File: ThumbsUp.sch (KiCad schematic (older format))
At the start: 170 parts, among them IC1 RP2040, IC2 W25Q128JVSIM, IC3 RP2040, IC4 W25Q128JVSIM, J1 Conn_01x04_Male, J10 Raiser_Male, J11 Raiser_Female, J12 Raiser_Male, J13 Raiser_Female, J14 Raiser_Male, J15 Raiser_Female, J16 Raiser_Male, J17 Raiser_Female, J18 Raiser_Male, J19 Raiser_Female, J2 Conn_01x04_Male, J20 Conn_01x04_Female, J21 Conn_01x04_Female, J22 Conn_01x04_Female, J23 Conn_01x04_Female, J24 Conn_01x04_Male, J25 Conn_01x04_Male, J26 Conn_01x04_Male, J27 Conn_01x04_Male, J28 Conn_01x04_Female, J29 Conn_01x04_Female, J3 Conn_01x04_Female, J30 Conn_01x04_Female, J31 Conn_01x04_Female, J32 USB_C_Receptacle_USB2.0, J33 Raiser_Male, J34 Raiser_Female, J35 Raiser_Male, J36 STX-3501-3N, J37 USB_C_Receptacle_USB2.0, J38 Raiser_Female, J39 Raiser_Male, J4 Conn_01x04_Male, J40 Raiser_Female, J41 Raiser_Male, J42 Raiser_Female, J43 Raiser_Male, J44 Raiser_Female, J45 Raiser_Male, J46 STX-3501-3N, J47 Raiser_Female, J48 Raiser_Male, J49 Raiser_Female, J5 Conn_01x04_Female, J50 Raiser_Male, J51 Raiser_Female, J52 Raiser_Male, J6 Conn_01x04_Male, J7 Conn_01x04_Male, J8 Conn_01x04_Male, J9 Raiser_Female, U1 AMS1117-3.3_SOT223, U2 AMS1117-3.3_SOT223, Y1 ABLS-12.000MHZ-B4-T, Y2 ABLS-12.000MHZ-B4-T

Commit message: Wired both RP2040s
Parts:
- MX1, MX10, MX11, MX12, MX13, MX14, MX15, MX16, MX17, MX18, MX19, MX2, MX20, MX21, MX22, MX23, MX24, MX25, MX26, MX27, MX28, MX29, MX3, MX30, MX31, MX32, MX33, MX34, MX35, MX36, MX37, MX38, MX39, MX4, MX40, MX41, MX42, MX43, MX44, MX45, MX46, MX47, MX48, MX49, MX5, MX50, MX51, MX52, MX53, MX54, MX55, MX56, MX57, MX58, MX6, MX7, MX8, MX9: footprint MX_Alps_Hybrid:MX-1U-NoLED_HotSwap -> keyswitches:MX-GLP2-HotSwap

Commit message: Layed out tracks on L2
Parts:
- J36, J46: value STX-3501-3N -> PJ-3200B; footprint STX-3501-3N:STX35013N -> random-keyboard-parts:PJ-3200B-4A
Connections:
- net +5V: now also J36.2, J46.2; no longer J36.3, J46.3
- net GND: now also J1.3 (Pin_3), J1.4 (Pin_4)
- net K_5: no longer J39.1 (Pin_1)
- net K_WIN: no longer J1.1 (Pin_1)
- net L-TIP: now also J36.3; no longer J36.2
- net R-TIP: now also J46.3; no longer J46.2
- no-connect marks 84 -> 91
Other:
- moved on the sheet: J36, J46
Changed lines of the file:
@@
 Wire Wire Line
 	8150 12700 8150 13500
-Connection ~ 8150 11900
-Wire Wire Line
-	8150 11900 8150 12700
 Connection ~ 10350 11850
 Wire Wire Line
@@
 	5200 5750 3950 5750
 Connection ~ 3950 5750
-Wire Wire Line
-	5200 8000 5200 7100
 Connection ~ 5200 7100
 $Comp
@@
 Text GLabel 7250 12100 0    50   Input ~ 0
 K_R
-Text GLabel 7950 12100 0    50   Input ~ 0
-K_T
 Text GLabel 7250 12900 0    50   Input ~ 0
 K_F
@@
 Connection ~ 14250 5700
 Wire Wire Line
-	14550 7950 15500 7950
-Wire Wire Line
 	15500 7950 15500 7050
 Connection ~ 15500 7050
@@
 	1    0    0    1
 $EndComp
-$Comp
-L STX-3501-3N:STX-3501-3N J46
-U 1 1 63F7C0D7
-P 15450 8050
-F 0 "J46" V 15804 8178 50  0000 L CNN
-F 1 "STX-3501-3N" V 15895 8178 50  0000 L CNN
-F 2 "STX-3501-3N:STX35013N" H 16100 8150 50  0001 L CNN
-F 3 "https://datasheet.datasheetarchive.com/originals/distributors/Datasheets_SAMA/ae9d1df0991347f2f81145ba35ca04dc.pdf" H 16100 8050 50  0001 L CNN
-F 4 "Phone Connectors 3.5mm S LUGS STEREO 3P THRU HOLE" H 16100 7950 50  0001 L CNN "Description"
-F 5 "5" H 16100 7850 50  0001 L CNN "Height"
-F 6 "Kycon" H 16100 7750 50  0001 L CNN "Manufacturer_Name"
-F 7 "STX-3501-3N" H 16100 7650 50  0001 L CNN "Manufacturer_Part_Number"
-F 8 "806-STX-3501-3N" H 16100 7550 50  0001 L CNN "Mouser Part Number"
-F 9 "https://www.mouser.co.uk/ProductDetail/Kycon/STX-3501-3N?qs=BBNwCsfFaznpJt4o1Jp%2FTg%3D%3D" H 16100 7450 50  0001 L CNN "Mouser Price/Stock"
-F 10 "" H 16100 7350 50  0001 L CNN "Arrow Part Number"
-F 11 "" H 16100 7250 50  0001 L CNN "Arrow Price/Stock"
-F 12 "" H 16100 7150 50  0001 L CNN "Mouser Testing Part Number"
-F 13 "" H 16100 7050 50  0001 L CNN "Mouser Testing Price/Stock"
-	1    15450 8050
-	0    1    1    0
-$EndComp
-$Comp
-L power:GND #PWR0149
-U 1 1 641658E3
-P 5500 8100
-F 0 "#PWR0149" H 5500 7850 50  0001 C CNN
-F 1 "GND" H 5505 7927 50  0000 C CNN
-F 2 "" H 5500 8100 50  0001 C CNN
-F 3 "" H 5500 8100 50  0001 C CNN
-	1    5500 8100
-	1    0    0    -1
-$EndComp
-Wire Wire Line
-	5300 8100 5500 8100
-Wire Wire Line
-	5300 8900 5500 8900
 Text GLabel 5050 8100 3    50   Input ~ 0
 L-TIP
-Text GLabel 5500 8100 2    50   Input ~ 0
-L-BASE
-Text GLabel 5500 8900 2    50   Input ~ 0
-L-RING1
-$Comp
-L power:GND #PWR0152
-U 1 1 64226D4D
-P 15700 8050
-F 0 "#PWR0152" H 15700 7800 50  0001 C CNN
-F 1 "GND" H 15705 7877 50  0000 C CNN
-F 2 "" H 15700 8050 50  0001 C CNN
-F 3 "" H 15700 8050 50  0001 C CNN
-	1    15700 8050
-	1    0    0    -1
-$EndComp
-Wire Wire Line
-	15450 8050 15700 8050
-Wire Wire Line
-	15450 8850 15700 8850
 Text GLabel 15100 8050 1    50   Input ~ 0
 R-TIP
-Text GLabel 15700 8050 2    50   Input ~ 0
-R-BASE
-Text GLabel 15700 8850 2    50   Input ~ 0
+Text GLabel 16250 7950 2    50   Input ~ 0
 R-RING1
 $Comp
@@
 $EndComp
 $Comp
-L power:+5V #PWR0147
-U 1 1 63F119E5
-P 5300 8900
-F 0 "#PWR0147" H 5300 8750 50  0001 C CNN
-F 1 "+5V" H 5315 9073 50  0000 C CNN
-F 2 "" H 5300 8900 50  0001 C CNN
-F 3 "" H 5300 8900 50  0001 C CNN
-	1    5300 8900
-	-1   0    0    1
-$EndComp
-Connection ~ 5300 8900
-Wire Wire Line
-	4250 8000 5200 8000
-$Comp
-L STX-3501-3N:STX-3501-3N J36
-U 1 1 63D573AD
-P 5300 8100
-F 0 "J36" V 5654 8228 50  0000 L CNN
-F 1 "STX-3501-3N" V 5745 8228 50  0000 L CNN
-F 2 "STX-3501-3N:STX35013N" H 5950 8200 50  0001 L CNN
-F 3 "https://datasheet.datasheetarchive.com/originals/distributors/Datasheets_SAMA/ae9d1df0991347f2f81145ba35ca04dc.pdf" H 5950 8100 50  0001 L CNN
-F 4 "Phone Connectors 3.5mm S LUGS STEREO 3P THRU HOLE" H 5950 8000 50  0001 L CNN "Description"
-F 5 "5" H 5950 7900 50  0001 L CNN "Height"
-F 6 "Kycon" H 5950 7800 50  0001 L CNN "Manufacturer_Name"
-F 7 "STX-3501-3N" H 5950 7700 50  0001 L CNN "Manufacturer_Part_Number"
-F 8 "806-STX-3501-3N" H 5950 7600 50  0001 L CNN "Mouser Part Number"
-F 9 "https://www.mouser.co.uk/ProductDetail/Kycon/STX-3501-3N?qs=BBNwCsfFaznpJt4o1Jp%2FTg%3D%3D" H 5950 7500 50  0001 L CNN "Mouser Price/Stock"
-F 10 "" H 5950 7400 50  0001 L CNN "Arrow Part Number"
-F 11 "" H 5950 7300 50  0001 L CNN "Arrow Price/Stock"
-F 12 "" H 5950 7200 50  0001 L CNN "Mouser Testing Part Number"
-F 13 "" H 5950 7100 50  0001 L CNN "Mouser Testing Price/Stock"
-	1    5300 8100
-	0    1    1    0
-$EndComp
-$Comp
 L power:+5V #PWR0148
 U 1 1 63FA1289
-P 15450 8850
-F 0 "#PWR0148" H 15450 8700 50  0001 C CNN
-F 1 "+5V" H 15465 9023 50  0000 C CNN
-F 2 "" H 15450 8850 50  0001 C CNN
-F 3 "" H 15450 8850 50  0001 C CNN
-	1    15450 8850
-	-1   0    0    1
+P 16150 7950
+F 0 "#PWR0148" H 16150 7800 50  0001 C CNN
+F 1 "+5V" H 16165 8123 50  0000 C CNN
+F 2 "" H 16150 7950 50  0001 C CNN
+F 3 "" H 16150 7950 50  0001 C CNN
+	1    16150 7950
+	1    0    0    -1
 $EndComp
-Connection ~ 15450 8850
 $Comp
 L Device:R R4
@@
 $EndComp
 Connection ~ 15000 8050
-Wire Wire Line
-	15000 8050 15350 8050
-Wire Wire Line
-	14550 8050 15000 8050
 Text GLabel 14550 7850 2    50   Input ~ 0
 K_BSPC
@@
 	8150 10800 8350 10800
 Connection ~ 8150 10800
-Wire Wire Line
-	8150 11100 8150 11900
 Text GLabel 6350 12400 2    50   Input ~ 0
 K_GRAVE
@@
 $EndComp
 Connection ~ 14500 15800
-Text GLabel 5600 15050 2    50   Input ~ 0
-K_WIN
 NoConn ~ 3450 9200
 NoConn ~ 3550 9200
@@
 	4250 8100 4850 8100
 Connection ~ 4850 8100
-Wire Wire Line
-	4850 8100 5200 8100
 Text GLabel 4250 7800 2    50   Input ~ 0
 K_3
@@
 Text GLabel 3750 9200 3    50   Input ~ 0
 K_4
-Text GLabel 20550 10400 3    50   Input ~ 0
-K_5
 $Comp
 L Connector:Conn_01x04_Female J51
@@
 Text GLabel 14550 8350 2    50   Input ~ 0
 K_THR
+$Comp
+L power:+5V #PWR0147
+U 1 1 63F119E5
+P 6000 8000
+F 0 "#PWR0147" H 6000 7850 50  0001 C CNN
+F 1 "+5V" H 6015 8173 50  0000 C CNN
+F 2 "" H 6000 8000 50  0001 C CNN
+F 3 "" H 6000 8000 50  0001 C CNN
+	1    6000 8000
+	1    0    0    -1
+$EndComp
+Text GLabel 6200 8000 2    50   Input ~ 0
+L-RING1
+Wire Wire Line
+	6000 8000 6200 8000
+Text GLabel 6200 8100 2    50   Input ~ 0
+L-BASE
+Wire Wire Line
+	6000 8100 6200 8100
+$Comp
+L power:GND #PWR0149
+U 1 1 641658E3
+P 6000 8100
+F 0 "#PWR0149" H 6000 7850 50  0001 C CNN
+F 1 "GND" H 6005 7927 50  0000 C CNN
+F 2 "" H 6000 8100 50  0001 C CNN
+F 3 "" H 6000 8100 50  0001 C CNN
+	1    6000 8100
+	1    0    0    -1
+$EndComp
+Wire Wire Line
+	5200 8000 5200 7100
+Wire Wire Line
+	4250 8000 5200 8000
+Wire Wire Line
+	4850 8100 5200 8100
+$Comp
+L power:GND #PWR0152
+U 1 1 64226D4D
+P 16150 8050
+F 0 "#PWR0152" H 16150 7800 50  0001 C CNN
+F 1 "GND" H 16155 7877 50  0000 C CNN
+F 2 "" H 16150 8050 50  0001 C CNN
+F 3 "" H 16150 8050 50  0001 C CNN
+	1    16150 8050
+	1    0    0    -1
+$EndComp
+Text GLabel 16250 8050 2    50   Input ~ 0
+R-BASE
+$Comp
+L STX-3501-3N:STX-3501-3N J36
+U 1 1 63D573AD
+P 6000 8100
+F 0 "J36" V 6354 8228 50  0000 L CNN
+F 1 "PJ-3200B" V 6445 8228 50  0000 L CNN
+F 2 "random-keyboard-parts:PJ-3200B-4A" H 6650 8200 50  0001 L CNN
+F 3 "https://datasheet.datasheetarchive.com/originals/distributors/Datasheets_SAMA/ae9d1df0991347f2f81145ba35ca04dc.pdf" H 6650 8100 50  0001 L CNN
+F 4 "Phone Connectors 3.5mm S LUGS STEREO 3P THRU HOLE" H 6650 8000 50  0001 L CNN "Description"
+F 5 "5" H 6650 7900 50  0001 L CNN "Height"
+F 6 "Kycon" H 6650 7800 50  0001 L CNN "Manufacturer_Name"
+F 7 "STX-3501-3N" H 6650 7700 50  0001 L CNN "Manufacturer_Part_Number"
+F 8 "806-STX-3501-3N" H 6650 7600 50  0001 L CNN "Mouser Part Number"
+F 9 "https://www.mouser.co.uk/ProductDetail/Kycon/STX-3501-3N?qs=BBNwCsfFaznpJt4o1Jp%2FTg%3D%3D" H 6650 7500 50  0001 L CNN "Mouser Price/Stock"
+F 10 "" H 6650 7400 50  0001 L CNN "Arrow Part Number"
+F 11 "" H 6650 7300 50  0001 L CNN "Arrow Price/Stock"
+F 12 "" H 6650 7200 50  0001 L CNN "Mouser Testing Part Number"
+F 13 "" H 6650 7100 50  0001 L CNN "Mouser Testing Price/Stock"
+	1    6000 8100
+	-1   0    0    1
+$EndComp
+Wire Wire Line
+	15000 8050 15350 8050
+Wire Wire Line
+	14550 8050 15000 8050
+Wire Wire Line
+	14550 7950 15500 7950
+$Comp
+L STX-3501-3N:STX-3501-3N J46
+U 1 1 63F7C0D7
+P 16150 8050
+F 0 "J46" V 16504 8178 50  0000 L CNN
+F 1 "PJ-3200B" V 16595 8178 50  0000 L CNN
+F 2 "random-keyboard-parts:PJ-3200B-4A" H 16800 8150 50  0001 L CNN
+F 3 "https://datasheet.datasheetarchive.com/originals/distributors/Datasheets_SAMA/ae9d1df0991347f2f81145ba35ca04dc.pdf" H 16800 8050 50  0001 L CNN
+F 4 "Phone Connectors 3.5mm S LUGS STEREO 3P THRU HOLE" H 16800 7950 50  0001 L CNN "Description"
+F 5 "5" H 16800 7850 50  0001 L CNN "Height"
+F 6 "Kycon" H 16800 7750 50  0001 L CNN "Manufacturer_Name"
+F 7 "STX-3501-3N" H 16800 7650 50  0001 L CNN "Manufacturer_Part_Number"
+F 8 "806-STX-3501-3N" H 16800 7550 50  0001 L CNN "Mouser Part Number"
+F 9 "https://www.mouser.co.uk/ProductDetail/Kycon/STX-3501-3N?qs=BBNwCsfFaznpJt4o1Jp%2FTg%3D%3D" H 16800 7450 50  0001 L CNN "Mouser Price/Stock"
+F 10 "" H 16800 7350 50  0001 L CNN "Arrow Part Number"
+F 11 "" H 16800 7250 50  0001 L CNN "Arrow Price/Stock"
+F 12 "" H 16800 7150 50  0001 L CNN "Mouser Testing Part Number"
+F 13 "" H 16800 7050 50  0001 L CNN "Mouser Testing Price/Stock"
+	1    16150 8050
+	-1   0    0    1
+$EndComp
+Wire Wire Line
+	16150 8050 16250 8050
+Connection ~ 16150 8050
+Wire Wire Line
+	16150 7950 16250 7950
+Connection ~ 16150 7950
+Connection ~ 6000 8000
+Connection ~ 6000 8100
+Text GLabel 7950 12100 0    50   Input ~ 0
+K_T
+NoConn ~ 20550 10400
+Wire Wire Line
+	8150 11100 8150 11900
+Connection ~ 8150 11900
+Wire Wire Line
+	8150 11900 8150 12700
+NoConn ~ 5600 15050
+NoConn ~ 5600 15150
+NoConn ~ 4900 15100
+NoConn ~ 4900 15200
+NoConn ~ 4900 15300
+NoConn ~ 4900 15400
+Wire Wire Line
+	5600 15250 5600 15350
+$Comp
+L power:GND #PWR?
+U 1 1 6612E548
+P 5600 15350
+F 0 "#PWR?" H 5600 15100 50  0001 C CNN
+F 1 "GND" H 5605 15177 50  0000 C CNN
+F 2 "" H 5600 15350 50  0001 C CNN
+F 3 "" H 5600 15350 50  0001 C CNN
+	1    5600 15350
+	1    0    0    -1
+$EndComp
+Connection ~ 5600 15350
 $EndSCHEMATC

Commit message: Layed out tracks on R2
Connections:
- net GND: now also J39.1 (Pin_1), J39.2 (Pin_2), J39.3 (Pin_3), J39.4 (Pin_4), J41.3 (Pin_3), J41.4 (Pin_4), J52.1 (Pin_1)
- no-connect marks 91 -> 84
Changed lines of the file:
@@
-	0    1    1    0
-$EndComp
-$Comp
-L Connector:Conn_01x04_Male J41
-U 1 1 63F4665F
-P 20450 11050
-F 0 "J41" V 20512 11194 50  0000 L CNN
-F 1 "Raiser_Male" V 20603 11194 50  0000 L CNN
-F 2 "Connector_PinHeader_2.54mm:PinHeader_1x04_P2.54mm_Vertical" H 20450 11050 50  0001 C CNN
-F 3 "~" H 20450 11050 50  0001 C CNN
-	1    20450 11050
 	0    1    1    0
 $EndComp
@@
 NoConn ~ 20450 10700
 NoConn ~ 20550 10700
-NoConn ~ 20250 11250
-NoConn ~ 20350 11250
 NoConn ~ 20450 11250
 NoConn ~ 20550 11250
@@
 NoConn ~ 20450 9850
 NoConn ~ 20550 9850
-NoConn ~ 20250 10400
-NoConn ~ 20350 10400
-NoConn ~ 20450 10400
 $Comp
 L Connector:Conn_01x04_Female J42
@@
 NoConn ~ 18700 11250
 NoConn ~ 18800 11250
-NoConn ~ 18900 11250
 $Comp
 L Connector:Conn_01x04_Female J49
@@
 Text GLabel 7950 12100 0    50   Input ~ 0
 K_T
-NoConn ~ 20550 10400
 Wire Wire Line
 	8150 11100 8150 11900
@@
 	5600 15250 5600 15350
 $Comp
-L power:GND #PWR?
+L power:GND #PWR0157
 U 1 1 6612E548
 P 5600 15350
-F 0 "#PWR?" H 5600 15100 50  0001 C CNN
+F 0 "#PWR0157" H 5600 15100 50  0001 C CNN
 F 1 "GND" H 5605 15177 50  0000 C CNN
 F 2 "" H 5600 15350 50  0001 C CNN
@@
 $EndComp
 Connection ~ 5600 15350
+$Comp
+L power:GND #PWR0158
+U 1 1 64F744BC
+P 18900 11250
+F 0 "#PWR0158" H 18900 11000 50  0001 C CNN
+F 1 "GND" H 18905 11077 50  0000 C CNN
+F 2 "" H 18900 11250 50  0001 C CNN
+F 3 "" H 18900 11250 50  0001 C CNN
+	1    18900 11250
+	1    0    0    -1
+$EndComp
+$Comp
+L Connector:Conn_01x04_Male J41
+U 1 1 63F4665F
+P 20450 11050
+F 0 "J41" V 20512 11194 50  0000 L CNN
+F 1 "Raiser_Male" V 20603 11194 50  0000 L CNN
+F 2 "Connector_PinHeader_2.54mm:PinHeader_1x04_P2.54mm_Vertical" H 20450 11050 50  0001 C CNN
+F 3 "~" H 20450 11050 50  0001 C CNN
+	1    20450 11050
+	0    1    1    0
+$EndComp
+$Comp
+L power:GND #PWR0161
+U 1 1 64F7DEB1
+P 20250 11250
+F 0 "#PWR0161" H 20250 11000 50  0001 C CNN
+F 1 "GND" H 20255 11077 50  0000 C CNN
+F 2 "" H 20250 11250 50  0001 C CNN
+F 3 "" H 20250 11250 50  0001 C CNN
+	1    20250 11250
+	1    0    0    -1
+$EndComp
+Wire Wire Line
+	20350 11250 20250 11250
+Connection ~ 20250 11250
+Wire Wire Line
+	20250 10400 20350 10400
+Connection ~ 20350 10400
+Wire Wire Line
+	20350 10400 20450 10400
+Connection ~ 20450 10400
+Wire Wire Line
+	20450 10400 20550 10400
+$Comp
+L power:GND #PWR?
+U 1 1 651A673D
+P 20250 10400
+F 0 "#PWR?" H 20250 10150 50  0001 C CNN
+F 1 "GND" H 20255 10227 50  0000 C CNN
+F 2 "" H 20250 10400 50  0001 C CNN
+F 3 "" H 20250 10400 50  0001 C CNN
+	1    20250 10400
+	1    0    0    -1
+$EndComp
+Connection ~ 20250 10400
 $EndSCHEMATC

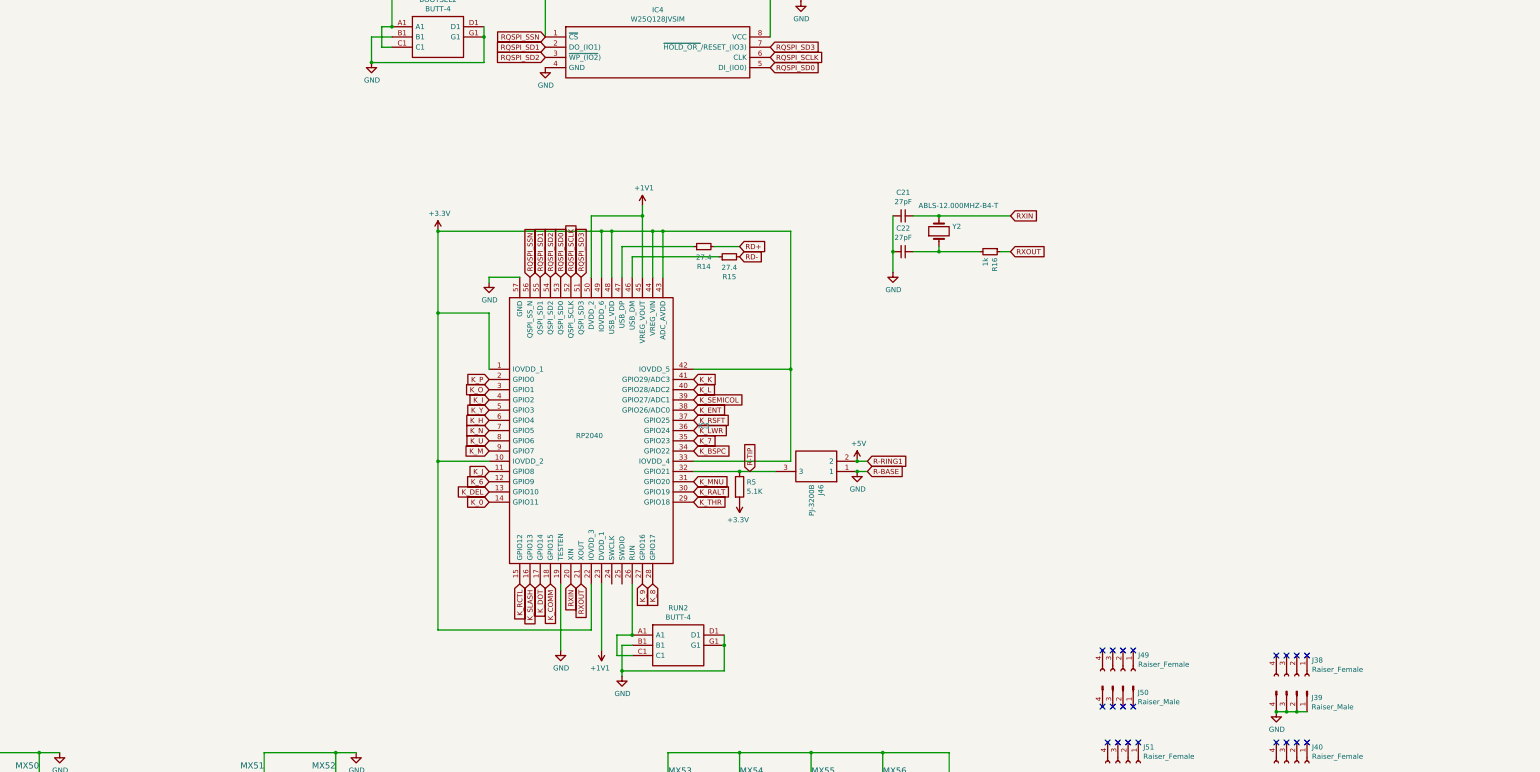
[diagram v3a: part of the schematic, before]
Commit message: Adding the 3key thumbclusters
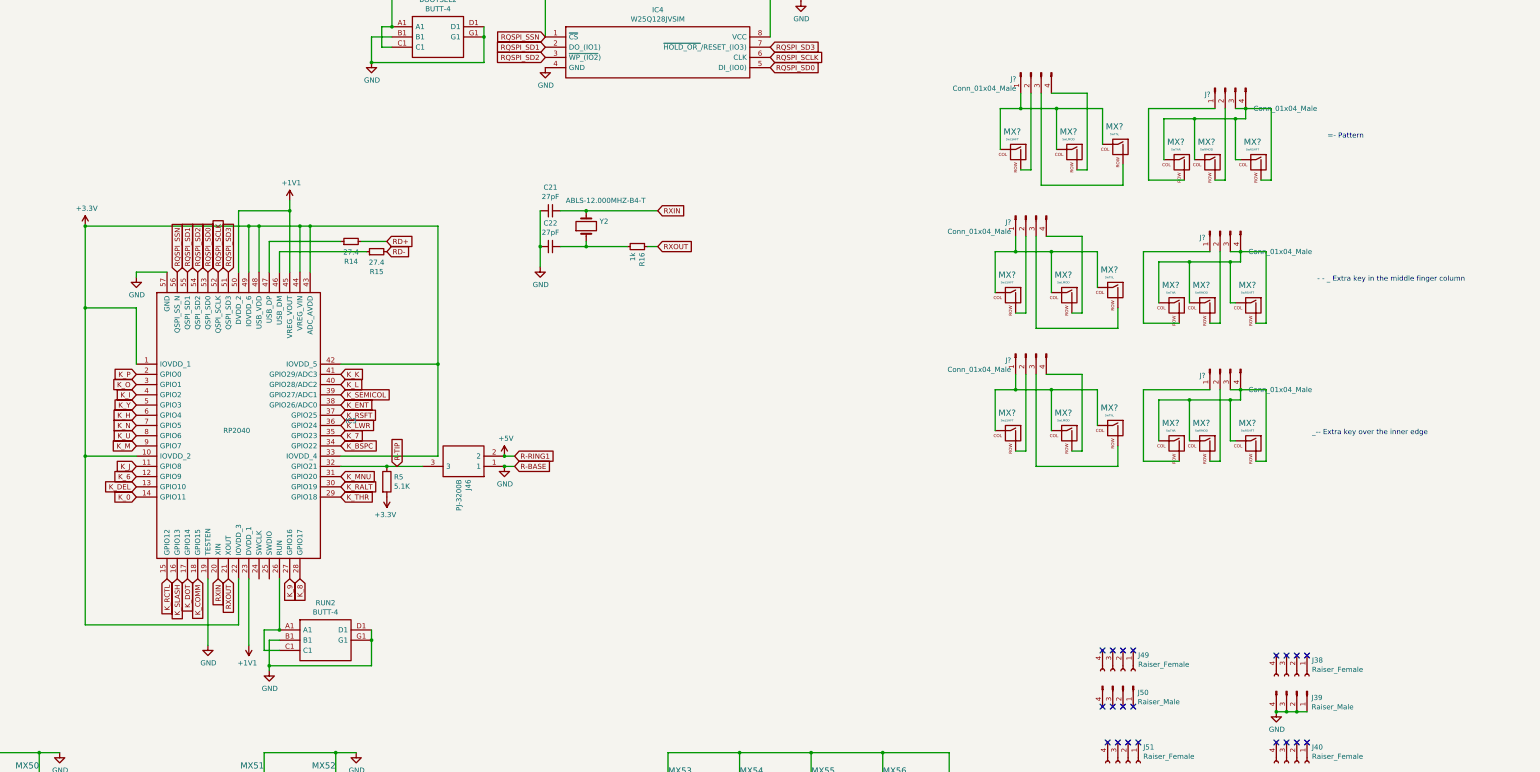
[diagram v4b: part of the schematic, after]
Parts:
- added J? (x6): Conn_01x04_Male, Connector_PinHeader_2.54mm:PinHeader_1x04_P2.54mm_Vertical, symbol Connector:Conn_01x04_Male
- added MX? (x3): SwLSHFT, keyswitches:MX-GLP2-HotSwap, symbol ThumbsUp-rescue:MX-NoLED-MX_Alps_Hybrid
- added MX? (x3): SwRMOD, keyswitches:MX-GLP2-HotSwap, symbol ThumbsUp-rescue:MX-NoLED-MX_Alps_Hybrid
- added MX? (x3): SwRSHFT, keyswitches:MX-GLP2-HotSwap, symbol ThumbsUp-rescue:MX-NoLED-MX_Alps_Hybrid
- added MX? (x3): SwThR, keyswitches:MX-GLP2-HotSwap, symbol ThumbsUp-rescue:MX-NoLED-MX_Alps_Hybrid
- added MX? (x3): SwThL, keyswitches:MX-GLP2-HotSwap, symbol ThumbsUp-rescue:MX-NoLED-MX_Alps_Hybrid
- added MX? (x3): SwLMOD, keyswitches:MX-GLP2-HotSwap, symbol ThumbsUp-rescue:MX-NoLED-MX_Alps_Hybrid
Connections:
- new net: J?.1 (Pin_1), MX?.1 (COL), MX?.1 (COL), MX?.1 (COL) (x3)
- new net: J?.2 (Pin_2), MX?.2 (ROW) (x6)
- new net: J?.3 (Pin_3), J?.4 (Pin_4), MX?.1 (COL), MX?.1 (COL), MX?.1 (COL), MX?.2 (ROW) (x3)
- new net: J?.1 (Pin_1), MX?.2 (ROW) (x3)
- new net: J?.3 (Pin_3), MX?.2 (ROW) (x3)
- new net: J?.4 (Pin_4), MX?.2 (ROW) (x3)
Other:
- note added: "- - _ Extra key in the middle finger column"
- note added: "=- Pattern"
- note added: "_-- Extra key over the inner edge"
- moved on the sheet: C21, C22, IC3, J46, R14, R15, R16, R5, RUN2, Y2
